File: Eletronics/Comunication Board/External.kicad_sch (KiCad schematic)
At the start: 7 parts, among them J2 Conn_01x10_Female

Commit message: edit communication board
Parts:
- removed BZ1: Buzzer, Buzzer_Beeper:Buzzer_12x9.5RM7.6, symbol Device:Buzzer
- removed J2: Conn_01x10_Female, Connector_IDC:IDC-Header_2x05_P2.54mm_Vertical, symbol Connector:Conn_01x10_Female
- removed R11: 330 Ω, Resistor_SMD:R_0603_1608Metric, symbol Device:R_Small
- added J2: Conn_01x14_Socket, symbol Connector:Conn_01x14_Socket
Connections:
- net GNDREF: now also J2.5 (Pin_5), J2.8 (Pin_8)
- net GPIO9: now also J2.11 (Pin_11)
- net RXD0: now also J2.6 (Pin_6)
- net SCL: now also J2.10 (Pin_10)
- net SDA: now also J2.9 (Pin_9)
- net SPI_CLK: now also J2.3 (Pin_3)
- net SPI_CS: now also J2.1 (Pin_1)
- net SPI_MISO: now also J2.4 (Pin_4)
- net SPI_MOSI: now also J2.2 (Pin_2)
- net TXD0: now also J2.7 (Pin_7)
- new net GPIO21: J2.12 (Pin_12)
- new net GPIO47: J2.14 (Pin_14)
- new net GPIO48: J2.13 (Pin_13)
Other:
- moved on the sheet: L1, R1, R8, R9

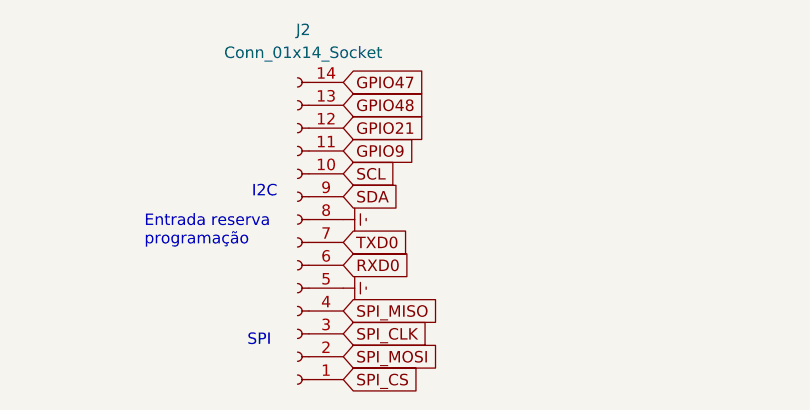
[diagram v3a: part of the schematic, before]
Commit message: modificacoes communication board
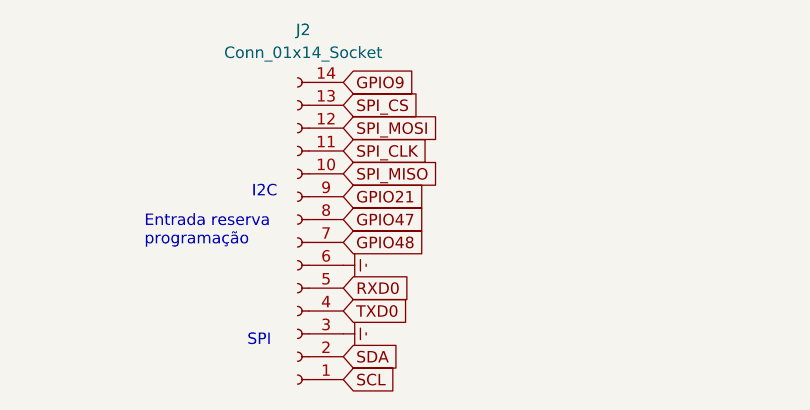
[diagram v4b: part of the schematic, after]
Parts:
- J2: footprint (none) -> Connector_IDC:IDC-Header_2x07_P2.54mm_Vertical
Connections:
- net GNDREF: now also J2.3 (Pin_3), J2.6 (Pin_6); no longer J2.5 (Pin_5), J2.8 (Pin_8)
- net GPIO21: now also J2.9 (Pin_9); no longer J2.12 (Pin_12)
- net GPIO47: now also J2.8 (Pin_8); no longer J2.14 (Pin_14)
- net GPIO48: now also J2.7 (Pin_7); no longer J2.13 (Pin_13)
- net GPIO9: now also J2.14 (Pin_14); no longer J2.11 (Pin_11)
- net RXD0: now also J2.5 (Pin_5); no longer J2.6 (Pin_6)
- net SCL: now also J2.1 (Pin_1); no longer J2.10 (Pin_10)
- net SDA: now also J2.2 (Pin_2); no longer J2.9 (Pin_9)
- net SPI_CLK: now also J2.11 (Pin_11); no longer J2.3 (Pin_3)
- net SPI_CS: now also J2.13 (Pin_13); no longer J2.1 (Pin_1)
- net SPI_MISO: now also J2.10 (Pin_10); no longer J2.4 (Pin_4)
- net SPI_MOSI: now also J2.12 (Pin_12); no longer J2.2 (Pin_2)
- net TXD0: now also J2.4 (Pin_4); no longer J2.7 (Pin_7)

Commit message: Mudanças esquematico
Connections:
- net GNDREF: no longer J2.6 (Pin_6)
- new net +5V: J2.6 (Pin_6)
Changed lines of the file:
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@@
-	)
-	(symbol
-		(lib_id "power:GNDREF")
-		(at 146.558 93.726 90)
-		(unit 1)
-		(exclude_from_sim no)
-		(in_bom yes)
-		(on_board yes)
-		(dnp no)
-		(fields_autoplaced yes)
-		(property "Reference" "#PWR03"
-			(at 152.908 93.726 0)
-			(effects
-				(font
-					(size 1.27 1.27)
-				)
-				(hide yes)
-			)
-		)
-		(property "Value" "GNDREF"
-			(at 151.384 93.726 0)
-			(effects
-				(font
-					(size 1.27 1.27)
-				)
-				(hide yes)
-			)
-		)
-		(property "Footprint" ""
-			(at 146.558 93.726 0)
-			(effects
-				(font
-					(size 1.27 1.27)
-				)
-				(hide yes)
-			)
-		)
-		(property "Datasheet" ""
-			(at 146.558 93.726 0)
-			(effects
-				(font
-					(size 1.27 1.27)
-				)
-				(hide yes)
-			)
-		)
-		(property "Description" ""
-			(at 146.558 93.726 0)
-			(effects
-				(font
-					(size 1.27 1.27)
-				)
-				(hide yes)
-			)
-		)
-		(pin "1"
-		)
-		(instances
-			(project "Comunication Board"
-				(path "/4c7888e1-33c4-4d9e-9379-8d84ea02e710/092dad48-0d23-47a5-8e6b-9ea28283eebf"
-					(reference "#PWR03")
-					(unit 1)
-				)
-			)
-		)
 	)
 	(symbol
@@
 					(unit 1)
 				)
+			)
+		)
+	)
+	(symbol
+		(lib_id "power:+5V")
+		(at 146.558 93.726 270)
+		(unit 1)
+		(exclude_from_sim no)
+		(in_bom yes)
+		(on_board yes)
+		(dnp no)
+		(property "Reference" "#PWR03"
+			(at 142.748 93.726 0)
+			(effects
+				(font
+					(size 1.27 1.27)
+				)
+				(hide yes)
+			)
+		)
+		(property "Value" "+5V"
+			(at 151.13 93.472 90)
+			(effects
+				(font
+					(size 1.27 1.27)
+				)
+			)
+		)
+		(property "Footprint" ""
+			(at 146.558 93.726 0)
+			(effects
+				(font
+					(size 1.27 1.27)
+				)
+				(hide yes)
+			)
+		)
+		(property "Datasheet" ""
+			(at 146.558 93.726 0)
+			(effects
+				(font
+					(size 1.27 1.27)
+				)
+				(hide yes)
+			)
+		)
+		(property "Description" ""
+			(at 146.558 93.726 0)
+			(effects
+				(font
+					(size 1.27 1.27)
+				)
+				(hide yes)
+			)
+		)
+		(pin "1"
+		)
+		(instances
+			(project "Comunication Board"
+				(path "/4c7888e1-33c4-4d9e-9379-8d84ea02e710/092dad48-0d23-47a5-8e6b-9ea28283eebf"
+					(reference "#PWR03")
+					(unit 1)
+				)

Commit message: Communication Board edit
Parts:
- removed J2: Conn_01x14_Socket, Connector_IDC:IDC-Header_2x07_P2.54mm_Vertical, symbol Connector:Conn_01x14_Socket
- added J2: Conn_01x16_Socket, Connector_IDC:IDC-Header_2x08_P2.54mm_Vertical, symbol Connector:Conn_01x16_Socket
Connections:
- net +5V: now also J2.15 (Pin_15)
- net GNDREF: now also J2.14 (Pin_14)
- net GPIO21: now also J2.7 (Pin_7)
- net GPIO47: now also J2.6 (Pin_6)
- net GPIO48: now also J2.5 (Pin_5)
- net GPIO9: now also J2.13 (Pin_13)
- net RXD0: now also J2.3 (Pin_3)
- net SCL: now also J2.1 (Pin_1)
- net SDA: now also J2.2 (Pin_2)
- net SPI_CLK: now also J2.10 (Pin_10)
- net SPI_CS: now also J2.12 (Pin_12)
- net SPI_MISO: now also J2.9 (Pin_9)
- net SPI_MOSI: now also J2.11 (Pin_11)
- net TXD0: now also J2.4 (Pin_4)
- new net GPIO14: J2.8 (Pin_8)
- no-connect marks 0 -> 1
